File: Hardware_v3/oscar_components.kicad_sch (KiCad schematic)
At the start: 71 parts, among them J1 SWD_Header, J10 MIDI_THROUGH, J11 USB_C_Receptacle, J12 Debug, J2 Eurorack_10_pin_power, J3 ChannelC_In, J4 ChannelA_In, J5 ChannelB_In, J6 ChC_Buff_Out, J7 ChA_Buff_Out, J8 ChB_Buff_Out, J9 MIDI_IN, SW1 Reset_Button, SW2 Menu_Button, SW3 Left_Encoder, SW4 Right_Encoder, U1 LT1117-3.3, U2 ILI9341_SPI_Daughterboard, U3 STM32F446RETx, U4 TL074, U5 MCP6004, U6 H11L1, Y1 8MHz

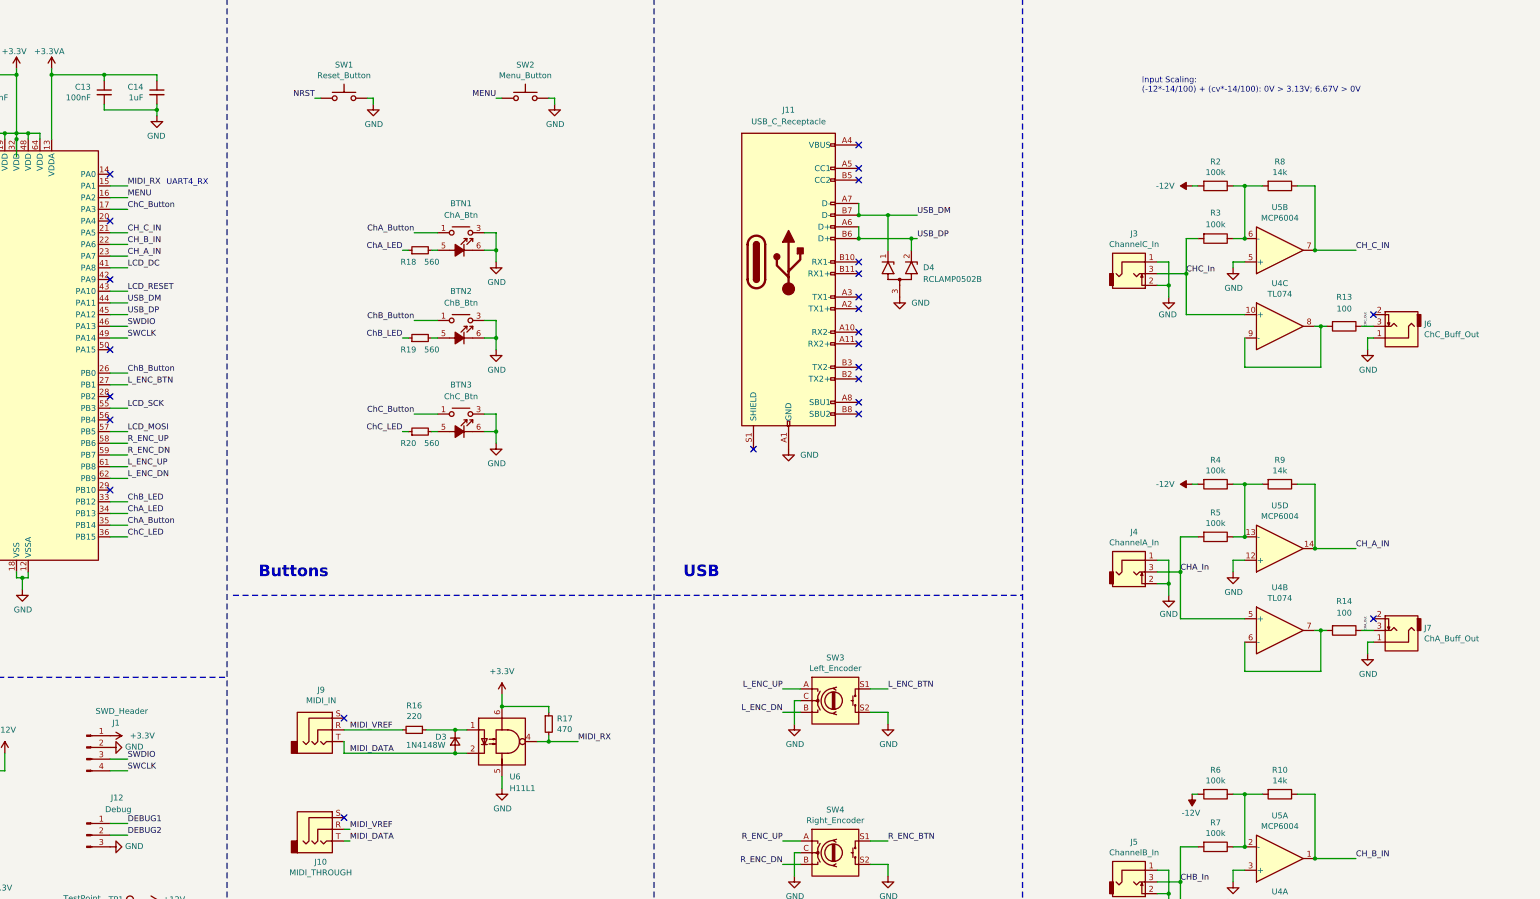
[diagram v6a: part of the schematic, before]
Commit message: V3 production files submitted to JLC
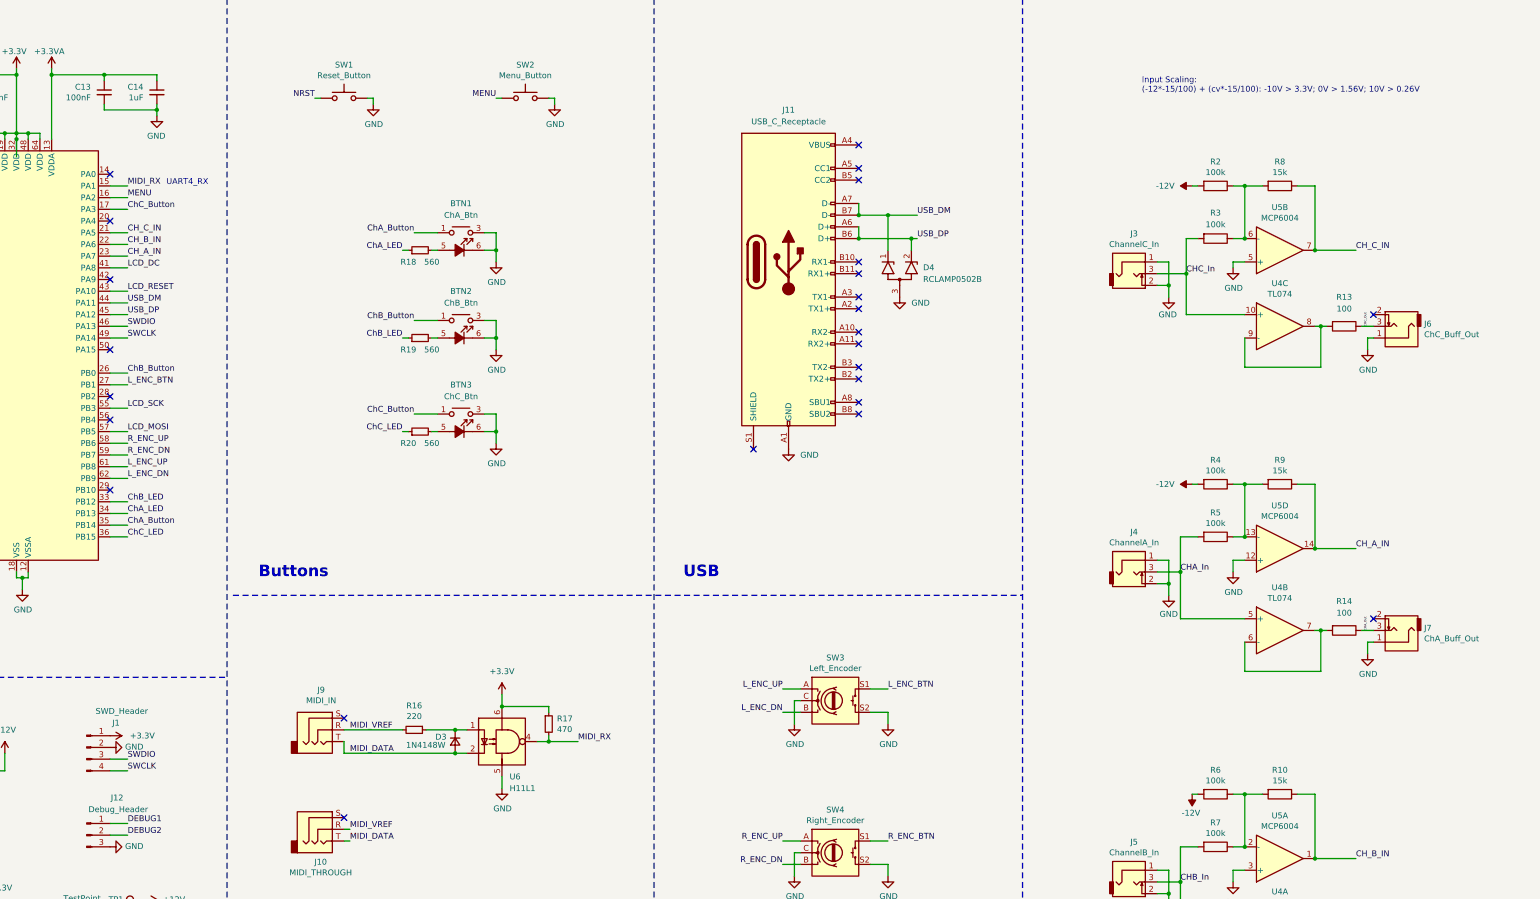
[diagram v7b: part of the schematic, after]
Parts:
- C4, C5: footprint Capacitor_SMD:C_0805_2012Metric -> Capacitor_SMD:C_0603_1608Metric_Pad1.08x0.95mm_HandSolder
- J12: value Debug -> Debug_Header
- R10, R8, R9: value 14k -> 15k
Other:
- note added: "Input Scaling: (-12*-15/100) + (cv*-15/100): -10V > 3.3V; 0V > 1.56V; 10V > 0.26V"
- note removed: "Input Scaling: (-12*-14/100) + (cv*-14/100): 0V > 3.13V; 6.67V > 0V"
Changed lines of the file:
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@@
 		)
 	)
-	(text "Input Scaling:\n(-12*-14/100) + (cv*-14/100): 0V > 3.13V; 6.67V > 0V\n"
+	(text "Input Scaling:\n(-12*-15/100) + (cv*-15/100): -10V > 3.3V; 0V > 1.56V; 10V > 0.26V\n"
 		(exclude_from_sim no)
 		(at 325.628 33.274 0)
@@
 			)
 		)
-		(property "Footprint" "Capacitor_SMD:C_0805_2012Metric"
+		(property "Footprint" "Capacitor_SMD:C_0603_1608Metric_Pad1.08x0.95mm_HandSolder"
 			(at 41.91 60.96 0)
 			(effects
@@
 			)
 		)
-		(property "Footprint" "Capacitor_SMD:C_0805_2012Metric"
+		(property "Footprint" "Capacitor_SMD:C_0603_1608Metric_Pad1.08x0.95mm_HandSolder"
 			(at 41.91 66.04 0)
 			(effects
@@
 			)
 		)
-		(property "Value" "14k"
+		(property "Value" "15k"
 			(at 355.6 50.3936 90)
 			(effects
@@
 			)
 		)
-		(property "Value" "14k"
+		(property "Value" "15k"
 			(at 355.6 115.1636 90)
 			(effects
@@
 			)
 		)
-		(property "Value" "14k"
+		(property "Value" "15k"
 			(at 355.6 182.4736 90)
 			(effects
@@
 			)
 		)
-		(property "Datasheet" "~"
+		(property "Datasheet" "https://www.mouser.co.uk/datasheet/2/15/SKHH-1370651.pdf"
 			(at 152.4 29.21 0)
 			(effects
@@
 			)
 		)
-		(property "Description" "Push button switch, generic, two pins"
+		(property "Description" "Push button switch, Alps SKHHDTA010"
 			(at 152.4 34.29 0)
 			(effects
@@
 			)
 		)
-		(property "Datasheet" "~"
+		(property "Datasheet" "https://www.mouser.co.uk/datasheet/2/54/PEC11R-777457.pdf"
 			(at 259.08 158.496 0)
 			(effects
@@
 			)
 		)
-		(property "Description" "Rotary encoder, dual channel, incremental quadrate outputs, with switch"
+		(property "Description" "Rotary encoder, PEC11R-4220F-S0024"
 			(at 259.08 165.1 0)
 			(effects
@@
 			)
 		)
-		(property "Datasheet" "~"
+		(property "Datasheet" "https://www.mouser.co.uk/datasheet/2/54/PEC11R-777457.pdf"
 			(at 259.08 191.516 0)
 			(effects
@@
 			)
 		)
-		(property "Description" "Rotary encoder, dual channel, incremental quadrate outputs, with switch"
+		(property "Description" "Rotary encoder, PEC11R-4220F-S0024"
 			(at 259.08 198.12 0)
 			(effects
@@
 			)
 		)
-		(property "Value" "Debug"
+		(property "Value" "Debug_Header"
 			(at 103.378 188.722 0)
 			(effects
@@
 			)
 		)
-		(property "Datasheet" "https://www.usb.org/sites/default/files/documents/usb_type-c.zip"
+		(property "Datasheet" "https://cdn.amphenol-cs.com/media/wysiwyg/files/drawing/12401951.pdf"
 			(at 252.73 69.85 0)
 			(effects
@@
 			)
 		)
-		(property "Datasheet" "~"
+		(property "Datasheet" "https://www.thonk.co.uk/wp-content/uploads/2021/12/LowProfileButton.pdf"
 			(at 177.8 77.47 0)
 			(effects
@@
 			)
 		)
-		(property "Description" ""
+		(property "Description" "Thonk Low Profile LED Buttons"
 			(at 177.8 85.09 0)
 			(effects
@@
 			)
 		)
-		(property "Datasheet" "~"
+		(property "Datasheet" "https://www.thonk.co.uk/wp-content/uploads/2021/12/LowProfileButton.pdf"
 			(at 177.8 58.42 0)
 			(effects
@@
 			)
 		)
-		(property "Description" ""
+		(property "Description" "Thonk Low Profile LED Buttons"
 			(at 177.8 66.04 0)
 			(effects
@@
 			)
 		)
-		(property "Datasheet" "~"
+		(property "Datasheet" "https://www.thonk.co.uk/wp-content/uploads/2021/12/LowProfileButton.pdf"
 			(at 177.8 97.79 0)
 			(effects
@@
 			)
 		)
-		(property "Description" ""
+		(property "Description" "Thonk Low Profile LED Buttons"
 			(at 177.8 105.41 0)
 			(effects
@@
 			)
 		)
-		(property "Datasheet" "~"
+		(property "Datasheet" "https://www.mouser.co.uk/datasheet/2/15/SKHH-1370651.pdf"
 			(at 191.77 29.21 0)
 			(effects
@@
 			)
 		)
-		(property "Description" "Push button switch, generic, two pins"
+		(property "Description" "Push button switch, Alps SKHHDTA010"
 			(at 191.77 34.29 0)
 			(effects
